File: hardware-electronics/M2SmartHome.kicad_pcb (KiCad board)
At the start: 2 copper layers, 22 x 76 mm, 207 parts, among them J1 M.2-Key-M-edge-connector, J2 Micro_SD_Card_Det_Hirose_DM3AT, J3 CONMHF1-SMD-T, J4 CONMHF1-SMD-T, U1 RTL8188FTV-VC-CG, U10 24AA04T-I_OT, U2 EMMC16G-MW28-01E10, U3 PI7C9X440SLBFDE, U4 24AA04T-I_OT, U5 CP2102N-A02-GQFN20, U6 24AA04T-I_OT, U7 EFR32MG21B020F1024IM32-B, U8 USB2244-AEZG-06, U9 USB2244-AEZG-06, Y1 ABM8-12.000MHZ-B2-T, Y2 ECS-240-10-47-CKM-TR, Y3 ECS-240-10-47-CKM-TR, Y5 ABM8-40.000MHZ-B2-T

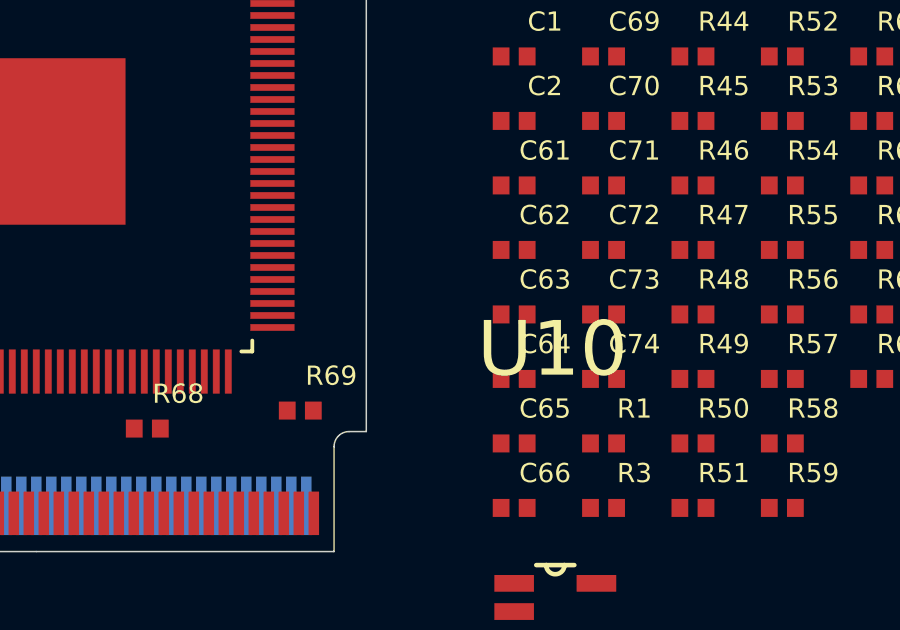
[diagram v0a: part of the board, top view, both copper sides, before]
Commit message: [#14] Add board stackup
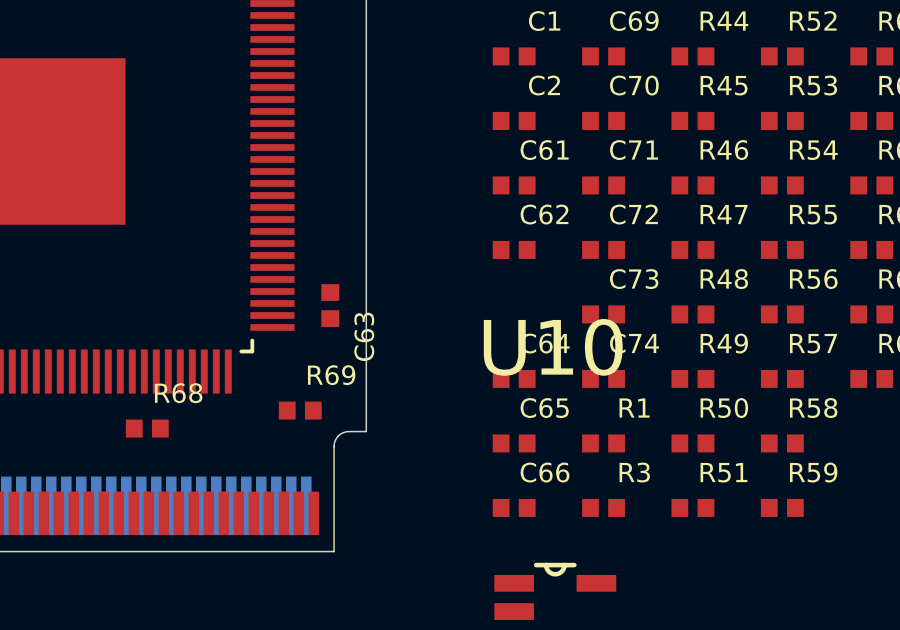
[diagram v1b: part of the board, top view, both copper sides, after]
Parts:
- moved C63 6.13 mm to (101.8, 157.8), turned to -90 degrees
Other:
- copper layers 2 -> 4
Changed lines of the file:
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@@
 	(generator_version "8.0")
 	(general
-		(thickness 1.6)
+		(thickness 0.7732)
 		(legacy_teardrops no)
 	)
@@
 	(layers
 		(0 "F.Cu" signal)
+		(1 "In1.Cu" signal)
+		(2 "In2.Cu" signal)
 		(31 "B.Cu" signal)
 		(32 "B.Adhes" user "B.Adhesive")
@@
 	)
 	(setup
+		(stackup
+			(layer "F.SilkS"
+				(type "Top Silk Screen")
+			)
+			(layer "F.Paste"
+				(type "Top Solder Paste")
+			)
+			(layer "F.Mask"
+				(type "Top Solder Mask")
+				(thickness 0.01)
+			)
+			(layer "F.Cu"
+				(type "copper")
+				(thickness 0.035)
+			)
+			(layer "dielectric 1"
+				(type "prepreg")
+				(thickness 0.0764)
+				(material "FR4")
+				(epsilon_r 4.5)
+				(loss_tangent 0.02)
+			)
+			(layer "In1.Cu"
+				(type "copper")
+				(thickness 0.0152)
+			)
+			(layer "dielectric 2"
+				(type "core")
+				(thickness 0.5)
+				(material "FR4")
+				(epsilon_r 4.5)
+				(loss_tangent 0.02)
+			)
+			(layer "In2.Cu"
+				(type "copper")
+				(thickness 0.0152)
+			)
+			(layer "dielectric 3"
+				(type "prepreg")
+				(thickness 0.0764)
+				(material "FR4")
+				(epsilon_r 4.5)
+				(loss_tangent 0.02)
+			)
+			(layer "B.Cu"
+				(type "copper")
+				(thickness 0.035)
+			)
+			(layer "B.Mask"
+				(type "Bottom Solder Mask")
+				(thickness 0.01)
+			)
+			(layer "B.Paste"
+				(type "Bottom Solder Paste")
+			)
+			(layer "B.SilkS"
+				(type "Bottom Silk Screen")
+			)
+			(copper_finish "ENIG")
+			(dielectric_constraints yes)
+			(edge_connector yes)
+		)
 		(pad_to_mask_clearance 0)
 		(allow_soldermask_bridges_in_footprints no)
@@
 		(at 100.8 161.3)
 		(property "Reference" "R69"
-			(at 1.032 -1.1564 360)
+			(at 1.032 -1.1564 0)
 			(layer "F.SilkS")
 			(effects
@@
 		)
 		(property "Value" "R_0_0402"
-			(at 3.8768 1.0936 360)
+			(at 3.8768 1.0936 0)
 			(layer "F.Fab")
 			(effects
@@
 		(at 107.675 100.965 90)
 		(property "Reference" "R66"
-			(at 1.032 -1.1564 270)
+			(at 1.032 -1.1564 -90)
 			(layer "F.SilkS")
 			(effects
@@
 		)
 		(property "Value" "R_66k5_0402"
-			(at 3.8768 1.0936 270)
+			(at 3.8768 1.0936 -90)
 			(layer "F.Fab")
 			(effects
@@
 		(at 95.7 161.9)
 		(property "Reference" "R68"
-			(at 1.032 -1.1564 360)
+			(at 1.032 -1.1564 0)
 			(layer "F.SilkS")
 			(effects
@@
 		)
 		(property "Value" "R_0_0402"
-			(at 3.8768 1.0936 360)
+			(at 3.8768 1.0936 0)
 			(layer "F.Fab")
 			(effects
@@
 	(footprint "M2SmartHomeFootprints:C_0402"
 		(layer "F.Cu")
-		(at 107.9278 158.0954)
+		(at 101.8 157.8 -90)
 		(property "Reference" "C63"
-			(at 1.032 -1.1564 0)
+			(at 1.032 -1.1564 90)
 			(layer "F.SilkS")
 			(effects
@@
 		)
 		(property "Value" "C_100n_0402"
-			(at 3.8768 1.0936 0)
+			(at 3.8768 1.0936 90)
 			(layer "F.Fab")
 			(effects
@@
 		)
 		(property "Footprint" "M2SmartHomeFootprints:C_0402"
-			(at 0 0 0)
+			(at 0 0 -90)
 			(unlocked yes)
 			(layer "F.Fab")
@@
 		)
 		(property "Datasheet" "https://www.murata.com/products/productdetail?partno=GRM155R61A104KE01%23"
-			(at 0 0 0)
+			(at 0 0 -90)
 			(unlocked yes)
 			(layer "F.Fab")
@@
 		)
 		(property "Description" "SMD Multilayer Ceramic Capacitor, 100 nF, 10 V, 0402 [1005 Metric], ±10%, X5R, GRM Series"
-			(at 0 0 0)
+			(at 0 0 -90)
 			(unlocked yes)
 			(layer "F.Fab")
@@
 		)
 		(property "MPN" "GRM155R61A104KE01D"
-			(at 0 0 0)
+			(at 0 0 -90)
 			(unlocked yes)
 			(layer "F.Fab")
@@
 		)
 		(property "Manufacturer" "Murata"
-			(at 0 0 0)
+			(at 0 0 -90)
 			(unlocked yes)
 			(layer "F.Fab")
@@
 		)
 		(property "License" "Apache-2.0"
-			(at 0 0 0)
+			(at 0 0 -90)
 			(unlocked yes)
 			(layer "F.Fab")
@@
 		)
 		(property "Author" "Your Name"
-			(at 0 0 0)
+			(at 0 0 -90)
 			(unlocked yes)
 			(layer "F.Fab")
@@
 		)
 		(property "Val" "100n"
-			(at 0 0 0)
+			(at 0 0 -90)
 			(unlocked yes)
 			(layer "F.Fab")
@@
 		)
 		(property "Voltage" "10V"
-			(at 0 0 0)
+			(at 0 0 -90)
 			(unlocked yes)
 			(layer "F.Fab")
@@
 		)
 		(property "Dielectric" "X5R"
-			(at 0 0 0)
+			(at 0 0 -90)
 			(unlocked yes)
 			(layer "F.Fab")
@@
 		(attr smd)
 		(fp_line
-			(start -0.965 -0.55)
-			(end 0.965 -0.55)
+			(start -0.965 0.55)
+			(end -0.965 -0.55)
 			(stroke
 				(width 0.05)
@@
 		)
 		(fp_line
-			(start -0.965 0.55)
-			(end -0.965 -0.55)
+			(start 0.965 0.55)
+			(end -0.965 0.55)
 			(stroke
 				(width 0.05)
@@
 		)
 		(fp_line
-			(start 0.965 -0.55)
-			(end 0.965 0.55)
+			(start -0.965 -0.55)
+			(end 0.965 -0.55)
 			(stroke
 				(width 0.05)
@@
 		)
 		(fp_line
-			(start 0.965 0.55)
-			(end -0.965 0.55)
+			(start 0.965 -0.55)
+			(end 0.965 0.55)
 			(stroke
 				(width 0.05)
@@
 		)
 		(fp_line
-			(start -0.5 -0.25)
-			(end 0.5 -0.25)
+			(start -0.5 0.25)
+			(end -0.5 -0.25)
 			(stroke
 				(width 0.127)
@@
 		)
 		(fp_line
-			(start -0.5 0.25)
-			(end -0.5 -0.25)
+			(start 0.5 0.25)
+			(end -0.5 0.25)
 			(stroke
 				(width 0.127)
@@
 		)
 		(fp_line
-			(start 0.5 -0.25)
-			(end 0.5 0.25)
+			(start -0.5 -0.25)
+			(end 0.5 -0.25)
 			(stroke
 				(width 0.127)
@@
 		)
 		(fp_line
-			(start 0.5 0.25)
-			(end -0.5 0.25)
+			(start 0.5 -0.25)
+			(end 0.5 0.25)
 			(stroke
 				(width 0.127)
@@
 		)
 		(pad "1" smd rect
-			(at -0.435 0)
+			(at -0.435 0 270)
 			(size 0.56 0.6)
 			(layers "F.Cu" "F.Paste" "F.Mask")
@@
 		)
 		(pad "2" smd rect
-			(at 0.435 0)
+			(at 0.435 0 270)
 			(size 0.56 0.6)
 			(layers "F.Cu" "F.Paste" "F.Mask")
@@
 		(at 90.1 162.2 90)
 		(property "Reference" "C80"
-			(at 1.032 -1.1564 270)
+			(at 1.032 -1.1564 -90)
 			(layer "F.SilkS")
 			(effects
@@
 		)
 		(property "Value" "C_220nF_0402"
-			(at 3.8768 1.0936 270)
+			(at 3.8768 1.0936 -90)
 			(layer "F.Fab")
 			(effects
@@
 		(at 91 114 90)
 		(property "Reference" "J2"
-			(at -4.41177 -12.95097 270)
+			(at -4.41177 -12.95097 -90)
 			(layer "F.SilkS")
 			(effects
@@
 		)
 		(property "Value" "Micro_SD_Card_Det_Hirose_DM3AT"
-			(at 3.85859 -10.78719 270)
+			(at 3.85859 -10.78719 -90)
 			(layer "F.Fab")
 			(effects
@@
 		)
 		(fp_text user "PCB Edge"
-			(at -2.36766 9.12 270)
+			(at -2.36766 9.12 -90)
 			(layer "F.Fab")
 			(effects
@@
 		(at 88.8 162.2 90)
 		(property "Reference" "C79"
-			(at 1.032 -1.1564 270)
+			(at 1.032 -1.1564 -90)
 			(layer "F.SilkS")
 			(effects
@@
 		)
 		(property "Value" "C_220nF_0402"
-			(at 3.8768 1.0936 270)
+			(at 3.8768 1.0936 -90)
 			(layer "F.Fab")
 			(effects

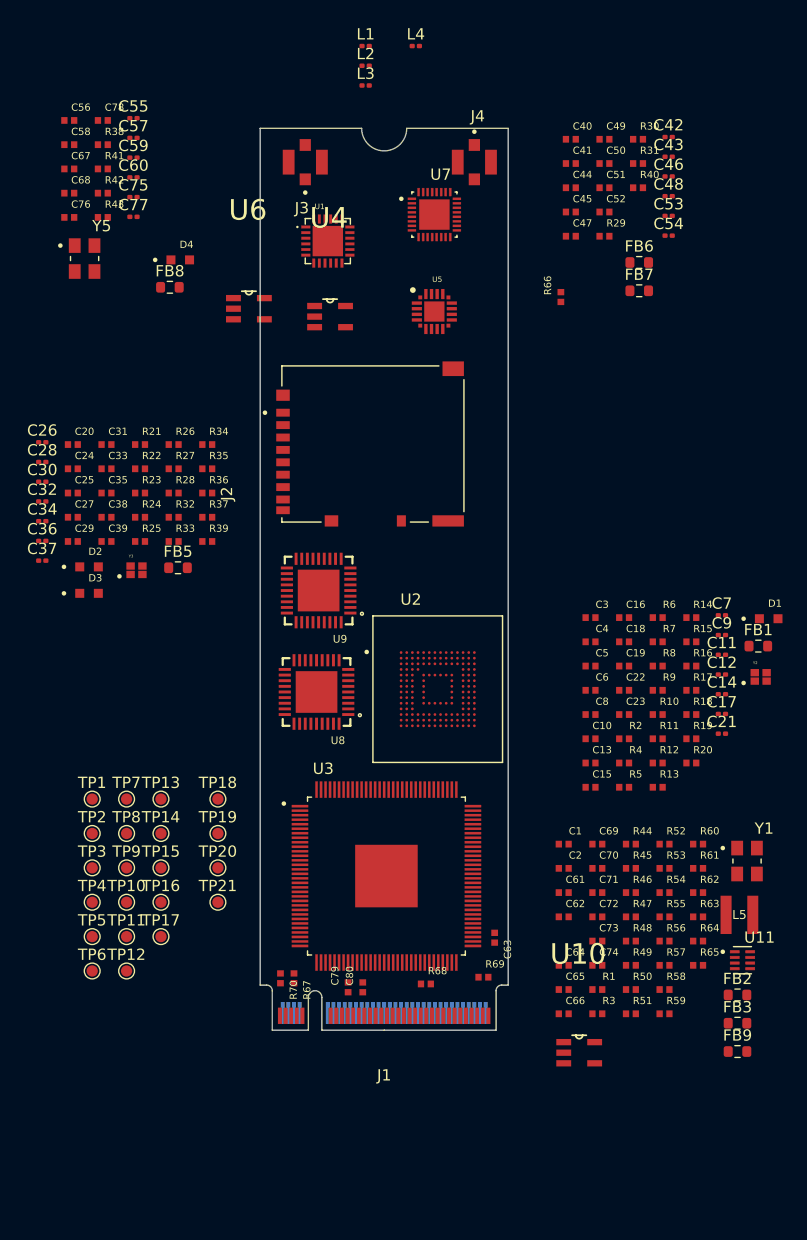
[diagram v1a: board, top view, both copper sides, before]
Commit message: [#13] WIP Placement PCIe bridge
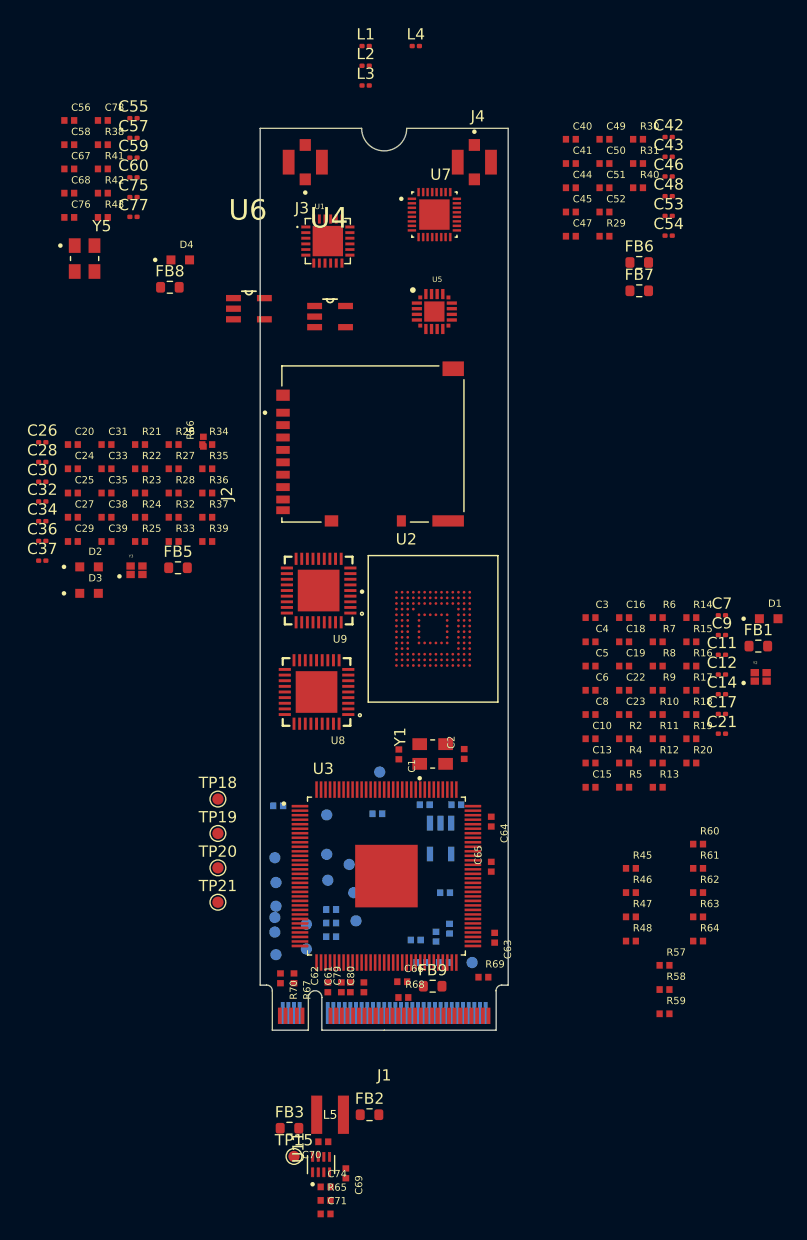
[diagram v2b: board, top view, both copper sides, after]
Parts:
- C72, C73, R1, R3, R44, R49, R50, R51, R52, R53, R54, R55, R56, TP1, TP10, TP11, TP12, TP13, TP14, TP16, TP17, TP2, TP3, TP4, TP5, TP6, TP7, TP8, TP9, U10: moved to B.Cu
- moved U11 41.5 mm to (86.4, 177.9), turned to 90 degrees
- moved FB3 40.8 mm to (83.6, 174.7)
- moved L5 40.4 mm to (87.2, 173.5)
- moved R65 39.1 mm to (86.8, 181.1)
- moved C71 37.3 mm to (86.8, 182.3)
- moved C69 36.7 mm to (88.6, 178.7), turned to -90 degrees
- moved R50 35.3 mm to (82.6, 146.1)
- moved C70 34.3 mm to (86.6, 175.9), turned to 180 degrees
- moved FB2 34.3 mm to (90.7, 173.5)
- moved R66 34.2 mm to (76.0, 113.8)
- moved C74 31.1 mm to (86.8, 179.9)
- moved TP6 31.0 mm to (91.6, 143.1), turned to 180 degrees
- moved Y1 29.5 mm to (96.3, 141.5), turned to 90 degrees
- moved TP15 28.2 mm to (84.0, 177.2)
- moved TP17 27.7 mm to (99.8, 160.0), turned to 180 degrees
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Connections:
- C70 pad 2: +3V3_Bridge -> Net-(U11-EN)

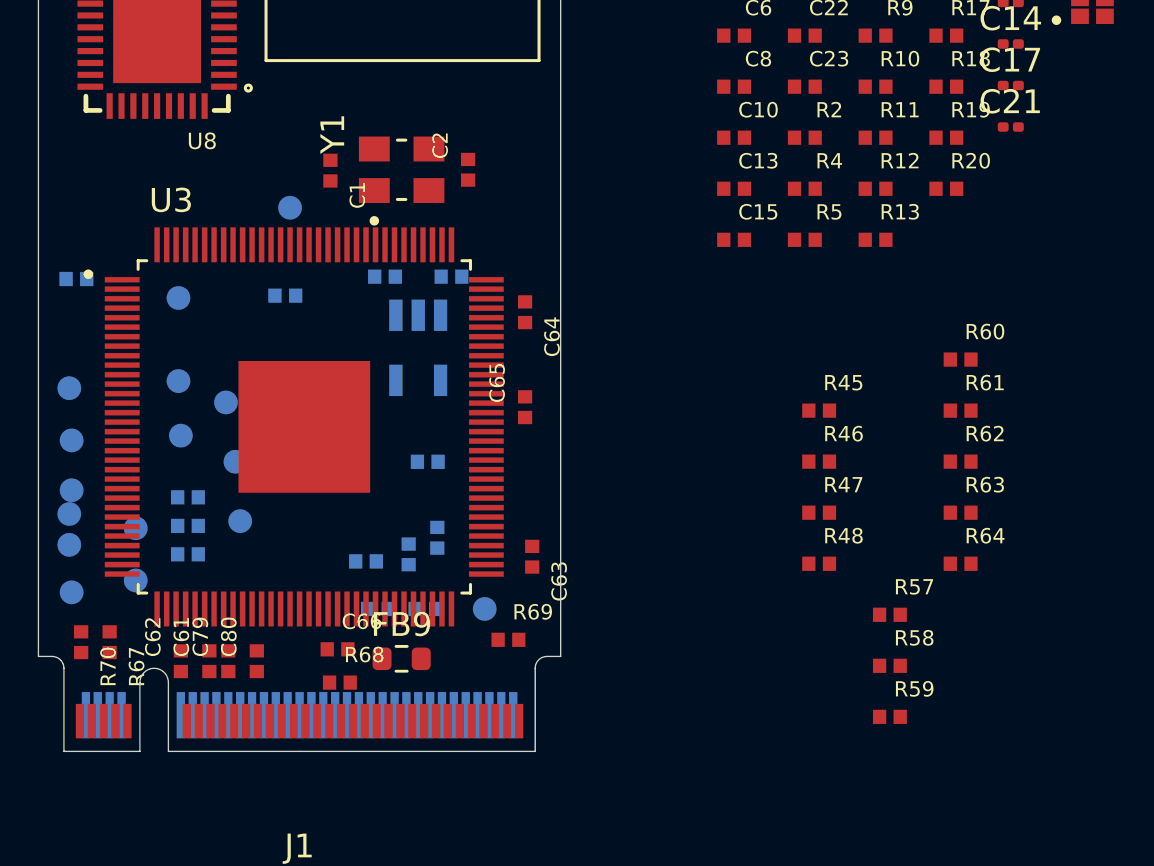
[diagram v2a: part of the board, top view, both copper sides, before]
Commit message: [#13] WIP Placement PCIe bridge
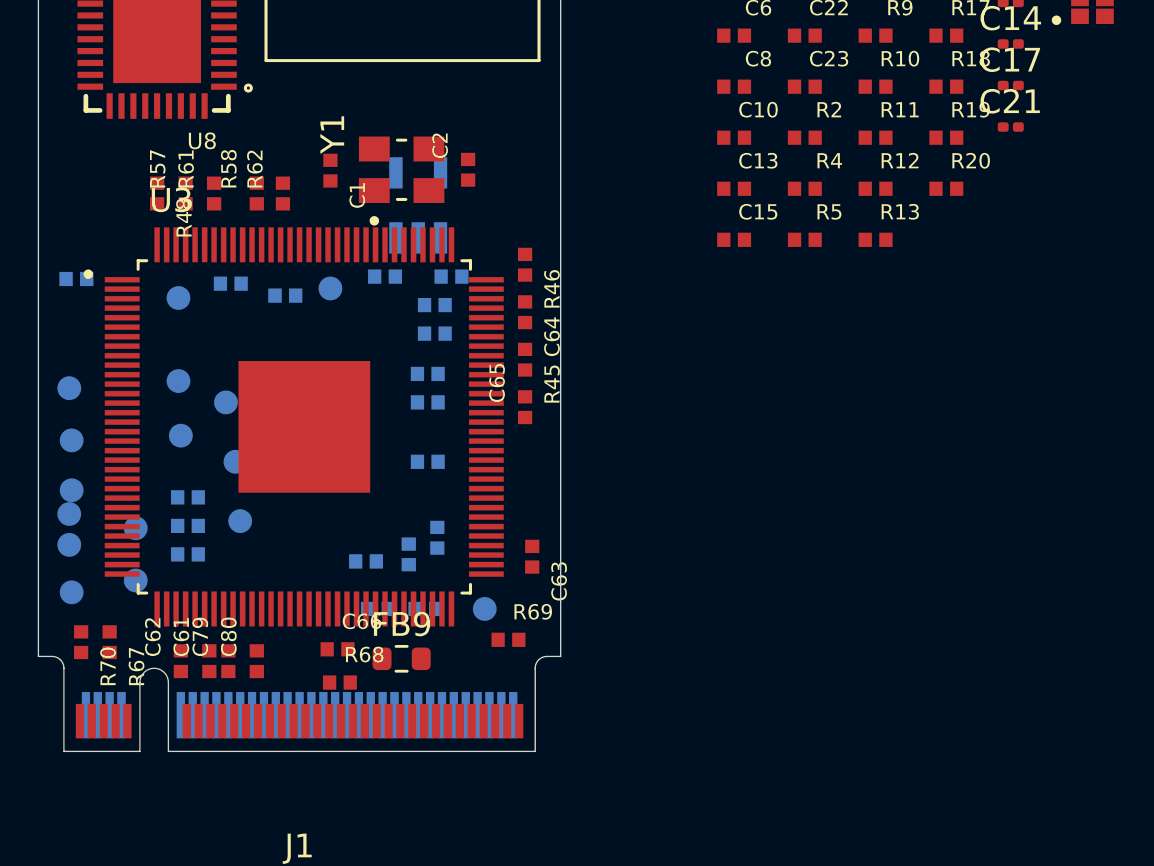
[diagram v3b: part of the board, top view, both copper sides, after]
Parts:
- R47, R59, R60, R63, R64: moved to B.Cu
- moved R57 34.6 mm to (87.2, 142.5), turned to 90 degrees
- moved R58 33.3 mm to (90.2, 142.5), turned to 90 degrees
- moved R61 32.8 mm to (88.4, 142.5), turned to 90 degrees
- moved R48 32.0 mm to (86.0, 142.5), turned to -90 degrees
- moved R62 30.7 mm to (91.3, 142.5), turned to 90 degrees
- moved R47 26.6 mm to (89.1, 146.3)
- moved R59 25.9 mm to (97.7, 147.2)
- moved R64 23.5 mm to (97.4, 151.3), turned to 180 degrees
- moved R63 23.4 mm to (97.7, 148.4)
- moved R60 22.5 mm to (97.4, 150.1), turned to 180 degrees
- moved R46 14.9 mm to (101.5, 145.5), turned to -90 degrees
- moved R45 12.6 mm to (101.5, 149.5), turned to -90 degrees
- moved U10 6.00 mm to (97.0, 143.0), turned to 90 degrees
- moved TP6 3.80 mm to (93.3, 146.5)
